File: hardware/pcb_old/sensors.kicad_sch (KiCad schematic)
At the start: 53 parts, among them J1 XT30PW-F, J12 Solar, J13 USB-C, U1 AP63205, U11 USBLC6, U12 TP5100, U7 CN3722, U8 MT3608

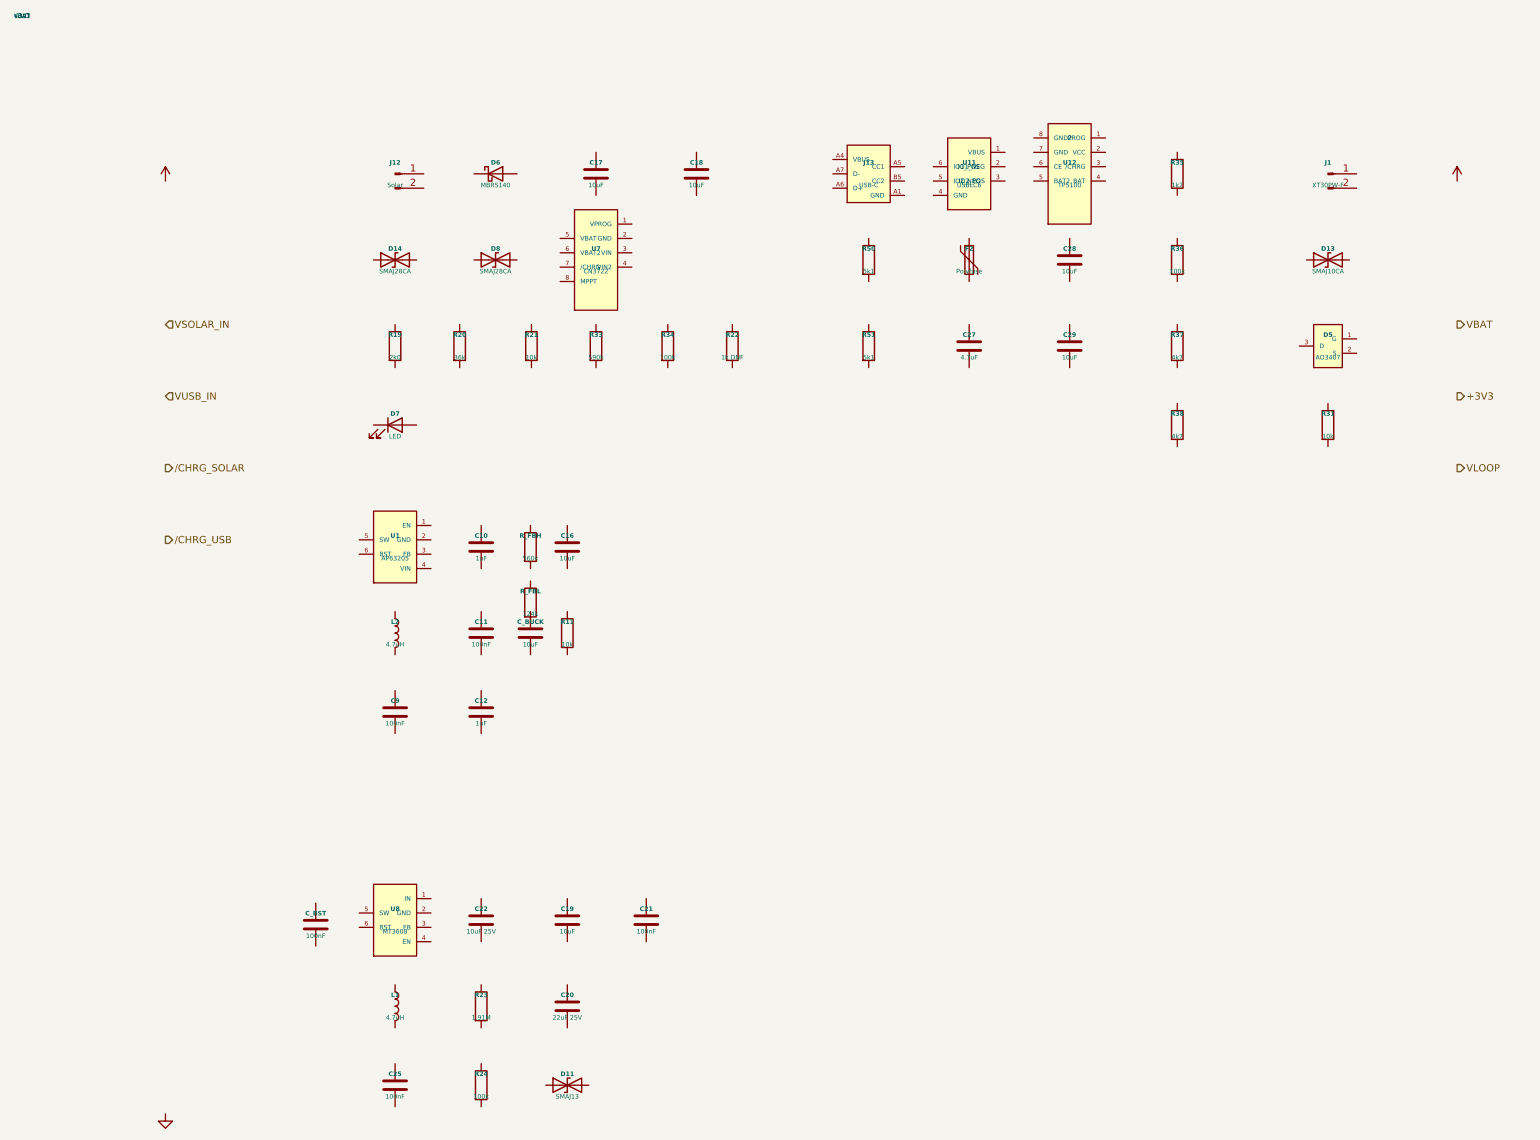
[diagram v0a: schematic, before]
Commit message: hw(pcb): fresh-start PCB — fix 4 critical schematic gaps, add wiring/placement docs
Archive old auto-generated PCB to hardware/pcb_old/. Start clean hardware/pcb/
with reference-only design documents for manual KiCad layout.

Critical electrical fixes:
- Add R_FBH (560kΩ) and R_FBL (124kΩ) symbols to power.kicad_sch — AP63205WU
  was missing its FB divider entirely; without it VOUT floats to rail and destroys
  the ESP32 on first power-on. Sets VOUT = 3.31V.
- Add R_DRDY (4.7kΩ) symbol to sensors.kicad_sch — ADS1115 ALERT/DRDY is
  open-drain and required an external pull-up; firmware was missing edges
  intermittently (root cause of bug fixed in adf7101).
- Add C_BST (100nF) symbol to power.kicad_sch — MT3608B BST→SW bootstrap
  cap is mandatory for gate driver; was ambiguous/missing.
- Add C_BUCK (10µF 0805) symbol to power.kicad_sch — AP63205WU primary output
  filter cap was absent from schematic.
- R33 already corrected from 604kΩ → 590kΩ (CN3722 CV 8.48V → 8.31V, safe for 2S).

New reference documents:
- bom_footprints.md — full BOM with KiCad 10 footprints, LCSC codes, PCBWay notes
- placement_constraints.md — must-be-near/apart rules from datasheets
- schematic_connections.md — net-by-net pin connectivity (authoritative wiring ref
  because schematic has symbols but zero wire connections yet)
- kicad_guide_eli5.md — step-by-step KiCad 10 setup guide including scripting console
- kicad_place_script.py — PCB editor scripting console auto-placement script
- senior_review_2026-05-25.md — senior reviewer report (BLOCKED, 4 CRITICAL)

CLAUDE.md: add electrical correctness gate to /improve cycle to catch missing
companion passives before tape-out.

Co-Authored-By: Claude Sonnet 4.6 <noreply@anthropic.com>
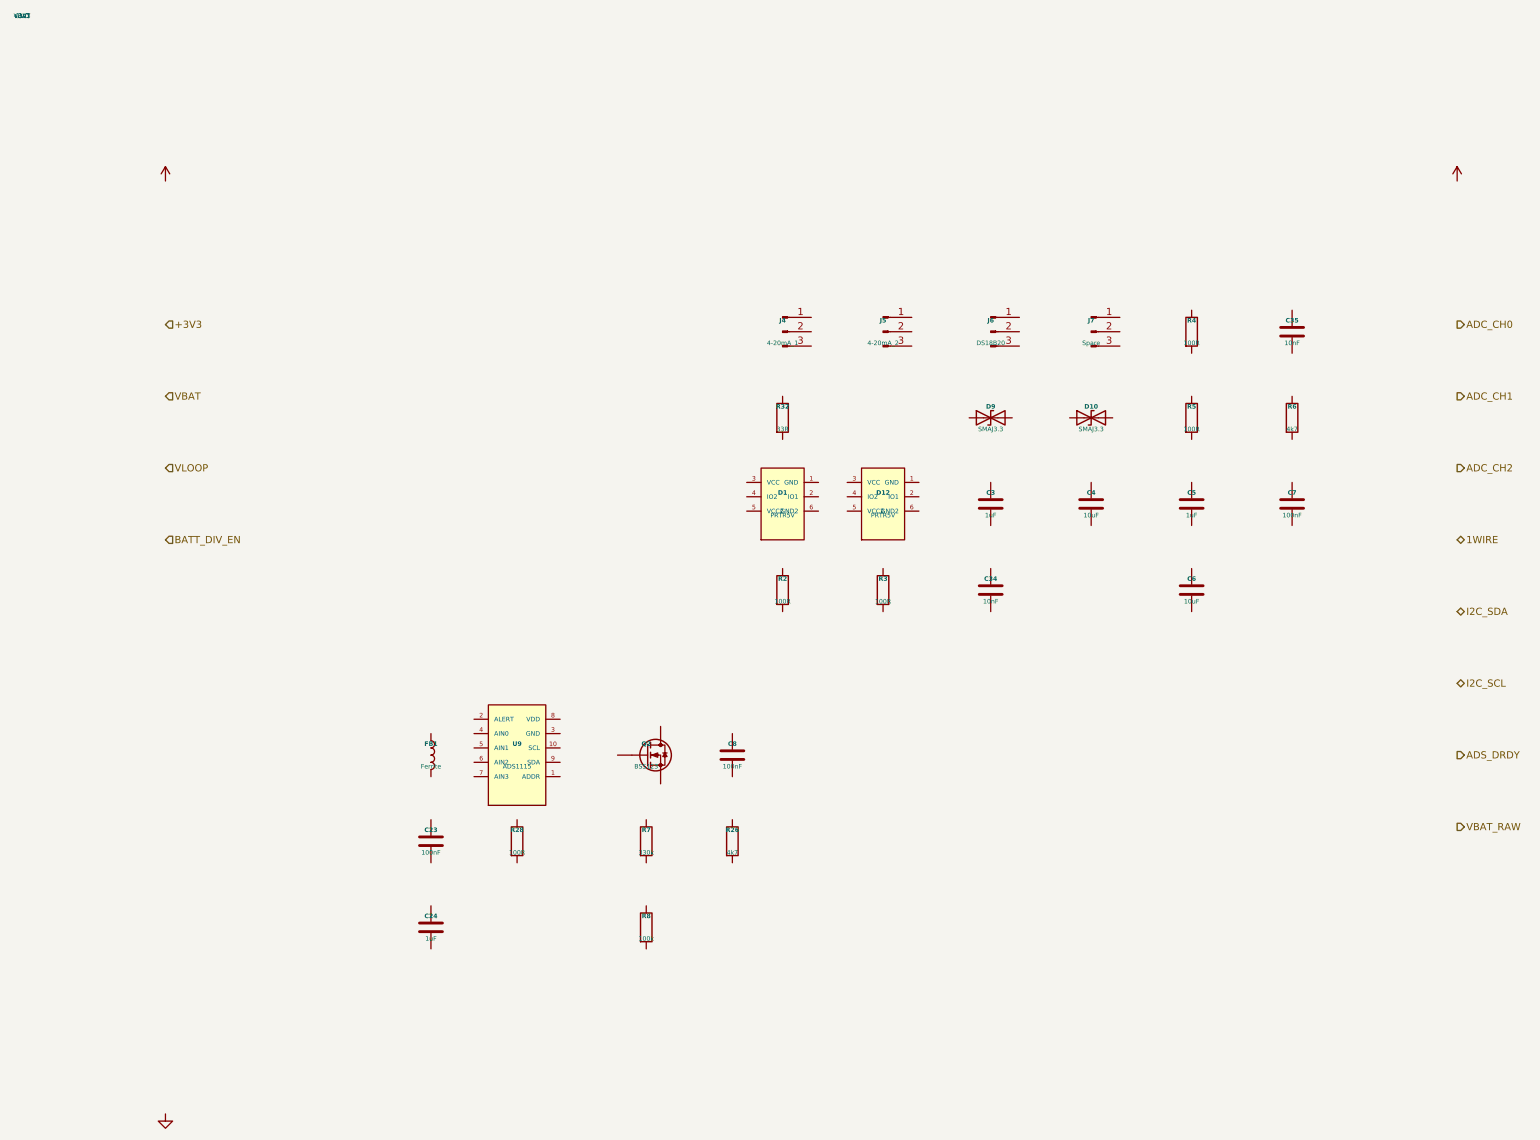
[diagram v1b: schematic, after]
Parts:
- removed C10, C12: 1uF, Capacitor_SMD:C_0402_1005Metric, symbol Device:C
- removed C11, C21, C25, C9, C_BST: 100nF, Capacitor_SMD:C_0402_1005Metric, symbol Device:C
- removed C16, C17, C18, C19, C28, C29, C_BUCK: 10uF, Capacitor_SMD:C_0805_2012Metric, symbol Device:C
- removed C20: 22uF 25V, Capacitor_SMD:C_1206_3216Metric, symbol Device:C
- removed C22: 10uF 25V, Capacitor_SMD:C_0805_2012Metric, symbol Device:C
- removed C27: 4.7uF, Capacitor_SMD:C_0805_2012Metric, symbol Device:C
- removed D11: SMAJ13, Diode_SMD:D_SMA, symbol Device:D_TVS
- removed D13: SMAJ10CA, Diode_SMD:D_SMA, symbol Device:D_TVS
- removed D14, D8: SMAJ28CA, Diode_SMD:D_SMA, symbol Device:D_TVS
- removed D5: AO3407, Package_TO_SOT_SMD:SOT-23, symbol welld:AO3407
- removed D6: MBRS140, Diode_SMD:D_SOD-123, symbol Device:D_Schottky
- removed D7: LED, LED_SMD:LED_0603_1608Metric, symbol Device:LED
- removed F2: Polyfuse, Fuse:Fuse_1206_3216Metric, symbol Device:Polyfuse
- removed J1: XT30PW-F, WellD:XT30PW-F_RightAngle, symbol Connector:Conn_01x02_Pin
- removed J12: Solar, TerminalBlock_Phoenix:TerminalBlock_Phoenix_PT-1,5-2-3.5-H_1x02_P3.50mm_Horizontal, symbol Connector:Conn_01x02_Pin
- removed J13: USB-C, Connector_USB:USB_C_Receptacle_GCT_USB4135-GF-A_6P_TopMnt_Horizontal, symbol welld:USB_C_Power
- removed L1, L2: 4.7uH, Inductor_SMD:L_Vishay_IFSC-1515AH_4x4x1.8mm, symbol Device:L
- removed R11, R21, R31: 10k, Resistor_SMD:R_0402_1005Metric, symbol Device:R
- removed R19: 2k0, Resistor_SMD:R_0402_1005Metric, symbol Device:R
- removed R20: 36k, Resistor_SMD:R_0402_1005Metric, symbol Device:R
- removed R22: 1k DNF, Resistor_SMD:R_0402_1005Metric, symbol Device:R
- removed R23: 1.91M, Resistor_SMD:R_0402_1005Metric, symbol Device:R
- removed R24, R34, R36: 100k, Resistor_SMD:R_0402_1005Metric, symbol Device:R
- removed R33: 590k, Resistor_SMD:R_0402_1005Metric, symbol Device:R
- removed R35: 1k2, Resistor_SMD:R_0402_1005Metric, symbol Device:R
- removed R37, R38: 4k7, Resistor_SMD:R_0402_1005Metric, symbol Device:R
- removed R50, R51: 5k1, Resistor_SMD:R_0402_1005Metric, symbol Device:R
- removed R_FBH: 560k, Resistor_SMD:R_0402_1005Metric, symbol Device:R
- removed R_FBL: 124k, Resistor_SMD:R_0402_1005Metric, symbol Device:R
- removed U1: AP63205, Package_TO_SOT_SMD:SOT-23-6, symbol welld:AP63205WU
- removed U11: USBLC6, Package_TO_SOT_SMD:SOT-23-6, symbol welld:USBLC6_2SC6
- removed U12: TP5100, Package_SO:SOIC-8_3.9x4.9mm_P1.27mm, symbol welld:TP5100
- removed U7: CN3722, Package_SO:SOIC-8_3.9x4.9mm_P1.27mm, symbol welld:CN3722
- removed U8: MT3608, Package_TO_SOT_SMD:SOT-23-6, symbol welld:MT3608B
- added C23, C7, C8: 100nF, Capacitor_SMD:C_0402_1005Metric, symbol Device:C
- added C24, C3, C5: 1uF, Capacitor_SMD:C_0402_1005Metric, symbol Device:C
- added C34, C35: 10nF, Capacitor_SMD:C_0402_1005Metric, symbol Device:C
- added C4, C6: 10uF, Capacitor_SMD:C_0805_2012Metric, symbol Device:C
- added D1, D12: PRTR5V, Package_TO_SOT_SMD:SOT-363_SC-70-6, symbol welld:PRTR5V0U2X
- added D10, D9: SMAJ3.3, Diode_SMD:D_SMA, symbol Device:D_TVS
- added FB1: Ferrite, Inductor_SMD:L_0402_1005Metric, symbol Device:L
- added J4: 4-20mA_1, TerminalBlock_Phoenix:TerminalBlock_Phoenix_PT-1,5-3-3.5-H_1x03_P3.50mm_Horizontal, symbol Connector:Conn_01x03_Pin
- added J5: 4-20mA_2, TerminalBlock_Phoenix:TerminalBlock_Phoenix_PT-1,5-3-3.5-H_1x03_P3.50mm_Horizontal, symbol Connector:Conn_01x03_Pin
- added J6: DS18B20, TerminalBlock_Phoenix:TerminalBlock_Phoenix_PT-1,5-3-3.5-H_1x03_P3.50mm_Horizontal, symbol Connector:Conn_01x03_Pin
- added J7: Spare, TerminalBlock_Phoenix:TerminalBlock_Phoenix_PT-1,5-3-3.5-H_1x03_P3.50mm_Horizontal, symbol Connector:Conn_01x03_Pin
- added Q2: BSS123, Package_TO_SOT_SMD:SOT-23, symbol Device:Q_NMOS
- added R2, R4: 100R, Resistor_SMD:R_0805_2012Metric, symbol Device:R
- added R26, R6: 4k7, Resistor_SMD:R_0402_1005Metric, symbol Device:R
- added R28, R3, R5: 100R, Resistor_SMD:R_0402_1005Metric, symbol Device:R
- added R32: 33R, Resistor_SMD:R_0402_1005Metric, symbol Device:R
- added R7: 330k, Resistor_SMD:R_0402_1005Metric, symbol Device:R
- added R8: 100k, Resistor_SMD:R_0402_1005Metric, symbol Device:R
- added U9: ADS1115, Package_SO:MSOP-10_3x3mm_P0.5mm, symbol welld:ADS1115
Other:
- title: WellD – Power -> WellD – Sensors
